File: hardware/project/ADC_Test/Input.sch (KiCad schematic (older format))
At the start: 51 parts, among them K601 HE3621A0510, K602 HE3621A0510, K603 HE3621A0510, Q601 BC847W, Q602 BC857W, U601 DG211, U602 DG211, U603 LTC1052, U604 TL061, U605 TL061, U606 TL431DBZ, U607 TL431DBZ, U608 LT5400-9k-1k

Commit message: Schematic design.
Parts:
- removed C? (x3): 10p, symbol Device:C
- removed Q? (x3): BC847W, Package_TO_SOT_SMD:SOT-323_SC-70, symbol Transistor_BJT:BC847W
- removed R? (x3): R, symbol Device:R
- added C601, C602, C603, C604, C605, C606, C607, C608, C609, C611, C612, C613, C614, C615, C616, C617, C619, C620, C622, C623, C624: 100n, Capacitor_SMD:C_0603_1608Metric_Pad1.05x0.95mm_HandSolder, symbol Device:C
- added R611, R613, R614, R615, R616, R617, R618: 620, Resistor_SMD:R_0603_1608Metric_Pad1.05x0.95mm_HandSolder, symbol Device:R
- added U603, U604, U605: SN74LVC1T45DBV, Package_TO_SOT_SMD:SOT-23-6, symbol Logic_LevelTranslator:SN74LVC1T45DBV
- added U606, U607: 74HCT595, Package_SO:TSSOP-16_4.4x5mm_P0.65mm, symbol 74xx:74HCT595
- C610: renamed from C601; footprint (none) -> Capacitor_SMD:C_1206_3216Metric_Pad1.42x1.75mm_HandSolder
- C618: renamed from C602; footprint (none) -> Capacitor_SMD:C_0603_1608Metric_Pad1.05x0.95mm_HandSolder
- C621: renamed from C603; footprint (none) -> Capacitor_SMD:C_0603_1608Metric_Pad1.05x0.95mm_HandSolder
- C625: renamed from C604; footprint (none) -> Capacitor_SMD:C_0603_1608Metric_Pad1.05x0.95mm_HandSolder
- C626: renamed from C605; footprint (none) -> Capacitor_SMD:C_0603_1608Metric_Pad1.05x0.95mm_HandSolder
- K601, K602, K603: footprint (none) -> ADC_Test:HE360_x-5050462-8
- L601: value INDUCTOR -> L0805R100MPWRT; footprint (none) -> Resistor_SMD:R_0805_2012Metric_Pad1.15x1.40mm_HandSolder
- R601, R602, R603, R604, R605, R606, R607: footprint (none) -> Resistor_SMD:R_1206_3216Metric_Pad1.42x1.75mm_HandSolder
- R608: renamed from R609; footprint (none) -> Resistor_SMD:R_1206_3216Metric_Pad1.42x1.75mm_HandSolder
- R609: renamed from R610; footprint (none) -> Resistor_SMD:R_1206_3216Metric_Pad1.42x1.75mm_HandSolder
- R610: renamed from R614; footprint (none) -> Resistor_SMD:R_1206_3216Metric_Pad1.42x1.75mm_HandSolder
- R612: value 1M -> 620; footprint (none) -> Resistor_SMD:R_0603_1608Metric_Pad1.05x0.95mm_HandSolder
- R619: renamed from R608; footprint (none) -> Resistor_SMD:R_0805_2012Metric_Pad1.15x1.40mm_HandSolder
- R620: renamed from R611; footprint (none) -> Resistor_SMD:R_0805_2012Metric_Pad1.15x1.40mm_HandSolder
- R621: renamed from R613; footprint (none) -> Resistor_SMD:R_0805_2012Metric_Pad1.15x1.40mm_HandSolder
- R622: renamed from R615; value 22 -> 22/.1%; footprint (none) -> Resistor_SMD:R_1206_3216Metric_Pad1.42x1.75mm_HandSolder
- R623: renamed from R616; value 12k -> 12k/.05%; footprint (none) -> Resistor_SMD:R_0603_1608Metric_Pad1.05x0.95mm_HandSolder
- R624: renamed from R617; footprint (none) -> Resistor_SMD:R_0805_2012Metric_Pad1.15x1.40mm_HandSolder
- R625: renamed from R618; footprint (none) -> Resistor_SMD:R_0805_2012Metric_Pad1.15x1.40mm_HandSolder
- R626: renamed from R619; footprint (none) -> Resistor_SMD:R_0805_2012Metric_Pad1.15x1.40mm_HandSolder
- R627: renamed from R620; footprint (none) -> Resistor_SMD:R_0805_2012Metric_Pad1.15x1.40mm_HandSolder
- R628: renamed from R621; footprint (none) -> Resistor_SMD:R_0805_2012Metric_Pad1.15x1.40mm_HandSolder
- R629: renamed from R622; footprint (none) -> Resistor_SMD:R_0805_2012Metric_Pad1.15x1.40mm_HandSolder
- R630: renamed from R623; value 620 -> 620/.05%; footprint (none) -> Resistor_SMD:R_0603_1608Metric_Pad1.05x0.95mm_HandSolder
- U601, U602: value DG211 -> DG211B; footprint (none) -> Package_SO:SOIC-16_3.9x9.9mm_P1.27mm; symbol ADC_TEST:DG211CJD -> ADC_TEST:DG211
- U601, U602: value DG211 -> DG211B; footprint (none) -> Package_SO:SOIC-16_3.9x9.9mm_P1.27mm
- U608: renamed from U603; footprint (none) -> Package_DIP:DIP-8_W7.62mm_Socket
- U609: renamed from U604; footprint (none) -> Package_SO:SOIC-8_3.9x4.9mm_P1.27mm
- U610: renamed from U605; footprint (none) -> Package_SO:SOIC-8_3.9x4.9mm_P1.27mm
- U613: renamed from U608; footprint (none) -> Package_SO:MSOP-8-1EP_3x3mm_P0.65mm_EP1.73x1.85mm_ThermalVias
- renumbered U606 to U611, U607 to U612
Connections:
- net labels added: +3.3VF, ADIN, DGNDF, K1_CTR, K2_CTR, K3_CTR, M1_2, M1_3, M1_4, M2_1, M2_2, M2_3, M2_4, SR_CLK, SR_DAT, SR_LAT
- net labels removed: AMP_OUT
- wire segments 165 -> 317
- no-connect marks 6 -> 12
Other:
- note added: "C1206C472FAGECTU"
- moved on the sheet: K601A, K601B, K602A, K602B, K603B, L601, R601, R602, R603, R604, R605, R606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

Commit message: Replaced TL061 with AD711.
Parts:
- removed U609, U610: TL061, Package_SO:SOIC-8_3.9x4.9mm_P1.27mm, symbol Amplifier_Operational:TL061
- added U609, U610: AD711, Package_SO:SOIC-8_3.9x4.9mm_P1.27mm, symbol ADC_TEST:AD711
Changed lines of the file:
@@
 Wire Wire Line
 	12450 4450 12900 4450
-$Comp
-L Amplifier_Operational:TL061 U610
-U 1 1 60D2E6C2
-P 12250 2350
-F 0 "U610" H 12350 2600 50  0000 L CNN
-F 1 "TL061" H 12350 2500 50  0000 L CNN
-F 2 "Package_SO:SOIC-8_3.9x4.9mm_P1.27mm" H 12300 2400 50  0001 C CNN
-F 3 "http://www.ti.com/lit/ds/symlink/tl061.pdf" H 12400 2500 50  0001 C CNN
-	1    12250 2350
-	1    0    0    -1
-$EndComp
 NoConn ~ 12250 2650
-NoConn ~ 12350 2650
 Wire Wire Line
 	11950 2450 11900 2450
@@
 	11450 6300 11900 6300
 $Comp
-L Amplifier_Operational:TL061 U609
-U 1 1 60E8A8A8
-P 10950 6300
-F 0 "U609" H 11000 6550 50  0000 L CNN
-F 1 "TL061" H 11000 6450 50  0000 L CNN
-F 2 "Package_SO:SOIC-8_3.9x4.9mm_P1.27mm" H 11000 6350 50  0001 C CNN
-F 3 "http://www.ti.com/lit/ds/symlink/tl061.pdf" H 11100 6450 50  0001 C CNN
-	1    10950 6300
-	1    0    0    -1
-$EndComp
-$Comp
 L Device:R R623
 U 1 1 60EAC183
@@
 Connection ~ 9450 6950
 NoConn ~ 10950 6600
-NoConn ~ 11050 6600
+NoConn ~ 10950 6000
 $Comp
 L ADC_TEST:+18VF #PWR0649
@@
 Text Notes 5900 6400 0    50   ~ 0
 C1206C472FAGECTU
+$Comp
+L ADC_TEST:AD711 U609
+U 1 1 5F856CB7
+P 10950 6300
+F 0 "U609" H 11100 6550 50  0000 L CNN
+F 1 "AD711" H 11100 6450 50  0000 L CNN
+F 2 "Package_SO:SOIC-8_3.9x4.9mm_P1.27mm" H 11000 6350 50  0001 C CNN
+F 3 "" H 11000 6450 50  0001 C CNN
+	1    10950 6300
+	1    0    0    -1
+$EndComp
+$Comp
+L ADC_TEST:AD711 U610
+U 1 1 5F86503E
+P 12250 2350
+F 0 "U610" H 12400 2600 50  0000 L CNN
+F 1 "AD711" H 12400 2500 50  0000 L CNN
+F 2 "Package_SO:SOIC-8_3.9x4.9mm_P1.27mm" H 12300 2400 50  0001 C CNN
+F 3 "" H 12300 2500 50  0001 C CNN
+	1    12250 2350
+	1    0    0    -1
+$EndComp
+NoConn ~ 12250 2050
 $EndSCHEMATC

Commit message: Schematic, PCB and BOM.
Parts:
- removed Q601: BC847W, Package_TO_SOT_SMD:SOT-323_SC-70, symbol Transistor_BJT:BC847W
- removed Q602: BC857W, Package_TO_SOT_SMD:SOT-323_SC-70, symbol Transistor_BJT:BC857W
- added Q601: BC847, Package_TO_SOT_SMD:SOT-23, symbol Transistor_BJT:BC847
- added Q602: BC857, Package_TO_SOT_SMD:SOT-23, symbol Transistor_BJT:BC857
- K601, K602, K603: footprint ADC_Test:HE360_x-5050462-8 -> ADC_TEST:HE360_x-5050462-8
- R601, R602, R603, R604, R605, R606, R607, R608, R609, R610: footprint Resistor_SMD:R_1206_3216Metric_Pad1.42x1.75mm_HandSolder -> Resistor_SMD:R_0805_2012Metric_Pad1.15x1.40mm_HandSolder
- R620, R621: value 240k -> 240k/.05%
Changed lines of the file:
@@
 P 7050 6100
 F 0 "R621" V 6843 6100 50  0000 C CNN
-F 1 "240k" V 6934 6100 50  0000 C CNN
+F 1 "240k/.05%" V 6934 6100 50  0000 C CNN
 F 2 "Resistor_SMD:R_0805_2012Metric_Pad1.15x1.40mm_HandSolder" V 6980 6100 50  0001 C CNN
 F 3 "~" H 7050 6100 50  0001 C CNN
@@
 P 6500 6100
 F 0 "R620" V 6293 6100 50  0000 C CNN
-F 1 "240k" V 6384 6100 50  0000 C CNN
+F 1 "240k/.05%" V 6384 6100 50  0000 C CNN
 F 2 "Resistor_SMD:R_0805_2012Metric_Pad1.15x1.40mm_HandSolder" V 6430 6100 50  0001 C CNN
 F 3 "~" H 6500 6100 50  0001 C CNN
@@
 F 0 "R601" V 2393 6750 50  0000 C CNN
 F 1 "1M" V 2484 6750 50  0000 C CNN
-F 2 "Resistor_SMD:R_1206_3216Metric_Pad1.42x1.75mm_HandSolder" V 2530 6750 50  0001 C CNN
+F 2 "Resistor_SMD:R_0805_2012Metric_Pad1.15x1.40mm_HandSolder" V 2530 6750 50  0001 C CNN
 F 3 "~" H 2600 6750 50  0001 C CNN
 	1    2600 6750
@@
 F 0 "R602" V 2693 6750 50  0000 C CNN
 F 1 "1M" V 2784 6750 50  0000 C CNN
-F 2 "Resistor_SMD:R_1206_3216Metric_Pad1.42x1.75mm_HandSolder" V 2830 6750 50  0001 C CNN
+F 2 "Resistor_SMD:R_0805_2012Metric_Pad1.15x1.40mm_HandSolder" V 2830 6750 50  0001 C CNN
 F 3 "~" H 2900 6750 50  0001 C CNN
 	1    2900 6750
@@
 F 0 "R603" V 2993 6750 50  0000 C CNN
 F 1 "1M" V 3084 6750 50  0000 C CNN
-F 2 "Resistor_SMD:R_1206_3216Metric_Pad1.42x1.75mm_HandSolder" V 3130 6750 50  0001 C CNN
+F 2 "Resistor_SMD:R_0805_2012Metric_Pad1.15x1.40mm_HandSolder" V 3130 6750 50  0001 C CNN
 F 3 "~" H 3200 6750 50  0001 C CNN
 	1    3200 6750
@@
 F 0 "R604" V 3293 6750 50  0000 C CNN
 F 1 "1M" V 3384 6750 50  0000 C CNN
-F 2 "Resistor_SMD:R_1206_3216Metric_Pad1.42x1.75mm_HandSolder" V 3430 6750 50  0001 C CNN
+F 2 "Resistor_SMD:R_0805_2012Metric_Pad1.15x1.40mm_HandSolder" V 3430 6750 50  0001 C CNN
 F 3 "~" H 3500 6750 50  0001 C CNN
 	1    3500 6750
@@
 F 0 "R605" V 3593 6750 50  0000 C CNN
 F 1 "1M" V 3684 6750 50  0000 C CNN
-F 2 "Resistor_SMD:R_1206_3216Metric_Pad1.42x1.75mm_HandSolder" V 3730 6750 50  0001 C CNN
+F 2 "Resistor_SMD:R_0805_2012Metric_Pad1.15x1.40mm_HandSolder" V 3730 6750 50  0001 C CNN
 F 3 "~" H 3800 6750 50  0001 C CNN
 	1    3800 6750
@@
 F 0 "R606" V 3893 6750 50  0000 C CNN
 F 1 "1M" V 3984 6750 50  0000 C CNN
-F 2 "Resistor_SMD:R_1206_3216Metric_Pad1.42x1.75mm_HandSolder" V 4030 6750 50  0001 C CNN
+F 2 "Resistor_SMD:R_0805_2012Metric_Pad1.15x1.40mm_HandSolder" V 4030 6750 50  0001 C CNN
 F 3 "~" H 4100 6750 50  0001 C CNN
 	1    4100 6750
@@
 F 0 "R607" V 4193 6750 50  0000 C CNN
 F 1 "1M" V 4284 6750 50  0000 C CNN
-F 2 "Resistor_SMD:R_1206_3216Metric_Pad1.42x1.75mm_HandSolder" V 4330 6750 50  0001 C CNN
+F 2 "Resistor_SMD:R_0805_2012Metric_Pad1.15x1.40mm_HandSolder" V 4330 6750 50  0001 C CNN
 F 3 "~" H 4400 6750 50  0001 C CNN
 	1    4400 6750
@@
 F 0 "R608" V 4493 6750 50  0000 C CNN
 F 1 "1M" V 4584 6750 50  0000 C CNN
-F 2 "Resistor_SMD:R_1206_3216Metric_Pad1.42x1.75mm_HandSolder" V 4630 6750 50  0001 C CNN
+F 2 "Resistor_SMD:R_0805_2012Metric_Pad1.15x1.40mm_HandSolder" V 4630 6750 50  0001 C CNN
 F 3 "~" H 4700 6750 50  0001 C CNN
 	1    4700 6750
@@
 F 0 "R609" V 4793 6750 50  0000 C CNN
 F 1 "1M" V 4884 6750 50  0000 C CNN
-F 2 "Resistor_SMD:R_1206_3216Metric_Pad1.42x1.75mm_HandSolder" V 4930 6750 50  0001 C CNN
+F 2 "Resistor_SMD:R_0805_2012Metric_Pad1.15x1.40mm_HandSolder" V 4930 6750 50  0001 C CNN
 F 3 "~" H 5000 6750 50  0001 C CNN
 	1    5000 6750
@@
 F 0 "R610" H 5320 7046 50  0000 L CNN
 F 1 "1M" H 5320 6955 50  0000 L CNN
-F 2 "Resistor_SMD:R_1206_3216Metric_Pad1.42x1.75mm_HandSolder" V 5180 7000 50  0001 C CNN
+F 2 "Resistor_SMD:R_0805_2012Metric_Pad1.15x1.40mm_HandSolder" V 5180 7000 50  0001 C CNN
 F 3 "~" H 5250 7000 50  0001 C CNN
 	1    5250 7000
@@
 Wire Wire Line
 	12650 2350 12550 2350
-$Comp
-L Transistor_BJT:BC857W Q602
-U 1 1 60D373EE
-P 12250 3200
-F 0 "Q602" H 12441 3154 50  0000 L CNN
-F 1 "BC857W" H 12441 3245 50  0000 L CNN
-F 2 "Package_TO_SOT_SMD:SOT-323_SC-70" H 12450 3125 50  0001 L CIN
-F 3 "http://www.infineon.com/dgdl/Infineon-BC857SERIES_BC858SERIES_BC859SERIES_BC860SERIES-DS-v01_01-en.pdf?fileId=db3a304314dca389011541da0e3a1661" H 12250 3200 50  0001 L CNN
-	1    12250 3200
-	-1   0    0    1
-$EndComp
 $Comp
 L ADC_TEST:-18VF #PWR0655
@@
 	13050 1350 13050 1600
 Connection ~ 13050 1600
-$Comp
-L Transistor_BJT:BC847W Q601
-U 1 1 60D5EC24
-P 12250 1600
-F 0 "Q601" H 12441 1646 50  0000 L CNN
-F 1 "BC847W" H 12441 1555 50  0000 L CNN
-F 2 "Package_TO_SOT_SMD:SOT-323_SC-70" H 12450 1525 50  0001 L CIN
-F 3 "http://www.infineon.com/dgdl/Infineon-BC847SERIES_BC848SERIES_BC849SERIES_BC850SERIES-DS-v01_01-en.pdf?fileId=db3a304314dca389011541d4630a1657" H 12250 1600 50  0001 L CNN
-	1    12250 1600
-	-1   0    0    -1
-$EndComp
 Wire Wire Line
 	12150 1800 12150 1900
@@
 F 0 "K601" V 2315 6100 50  0000 C CNN
 F 1 "HE3621A0510" V 2224 6100 50  0000 C CNN
-F 2 "ADC_Test:HE360_x-5050462-8" H 2350 6050 50  0001 C CNN
+F 2 "ADC_TEST:HE360_x-5050462-8" H 2350 6050 50  0001 C CNN
 F 3 "" H 2350 6050 50  0001 C CNN
 	1    2100 6100
@@
 F 0 "K601" H 2478 10396 50  0000 L CNN
 F 1 "HE3621A0510" H 2478 10305 50  0000 L CNN
-F 2 "ADC_Test:HE360_x-5050462-8" H 2650 10300 50  0001 C CNN
+F 2 "ADC_TEST:HE360_x-5050462-8" H 2650 10300 50  0001 C CNN
 F 3 "" H 2650 10300 50  0001 C CNN
 	2    2400 10350
@@
 F 0 "K602" V 2315 6750 50  0000 C CNN
 F 1 "HE3621A0510" V 2224 6750 50  0000 C CNN
-F 2 "ADC_Test:HE360_x-5050462-8" H 2350 6700 50  0001 C CNN
+F 2 "ADC_TEST:HE360_x-5050462-8" H 2350 6700 50  0001 C CNN
 F 3 "" H 2350 6700 50  0001 C CNN
 	1    2100 6750
@@
 F 0 "K602" H 3278 10396 50  0000 L CNN
 F 1 "HE3621A0510" H 3278 10305 50  0000 L CNN
-F 2 "ADC_Test:HE360_x-5050462-8" H 3450 10300 50  0001 C CNN
+F 2 "ADC_TEST:HE360_x-5050462-8" H 3450 10300 50  0001 C CNN
 F 3 "" H 3450 10300 50  0001 C CNN
 	2    3200 10350
@@
 F 0 "K603" H 5328 6446 50  0000 L CNN
 F 1 "HE3621A0510" H 5328 6355 50  0000 L CNN
-F 2 "ADC_Test:HE360_x-5050462-8" H 5500 6350 50  0001 C CNN
+F 2 "ADC_TEST:HE360_x-5050462-8" H 5500 6350 50  0001 C CNN
 F 3 "" H 5500 6350 50  0001 C CNN
 	1    5250 6400
@@
 F 0 "K603" H 4078 10396 50  0000 L CNN
 F 1 "HE3621A0510" H 4078 10305 50  0000 L CNN
-F 2 "ADC_Test:HE360_x-5050462-8" H 4250 10300 50  0001 C CNN
+F 2 "ADC_TEST:HE360_x-5050462-8" H 4250 10300 50  0001 C CNN
 F 3 "" H 4250 10300 50  0001 C CNN
 	2    4000 10350
@@
 $EndComp
 NoConn ~ 12250 2050
+$Comp
+L Transistor_BJT:BC847 Q601
+U 1 1 5F8E554E
+P 12250 1600
+F 0 "Q601" H 12441 1646 50  0000 L CNN
+F 1 "BC847" H 12441 1555 50  0000 L CNN
+F 2 "Package_TO_SOT_SMD:SOT-23" H 12450 1525 50  0001 L CIN
+F 3 "http://www.infineon.com/dgdl/Infineon-BC847SERIES_BC848SERIES_BC849SERIES_BC850SERIES-DS-v01_01-en.pdf?fileId=db3a304314dca389011541d4630a1657" H 12250 1600 50  0001 L CNN
+	1    12250 1600
+	-1   0    0    -1
+$EndComp
+$Comp
+L Transistor_BJT:BC857 Q602
+U 1 1 5F8EBE07
+P 12250 3200
+F 0 "Q602" H 12441 3154 50  0000 L CNN
+F 1 "BC857" H 12441 3245 50  0000 L CNN
+F 2 "Package_TO_SOT_SMD:SOT-23" H 12450 3125 50  0001 L CIN
+F 3 "http://www.fairchildsemi.com/ds/BC/BC856.pdf" H 12250 3200 50  0001 L CNN
+	1    12250 3200
+	-1   0    0    1
+$EndComp
 $EndSCHEMATC

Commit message: PCB design
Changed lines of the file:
@@
-$Comp
-L ADC_TEST:HE3621A0510 K603
-U 1 1 6104A372
-P 5250 6400
-F 0 "K603" H 5328 6446 50  0000 L CNN
-F 1 "HE3621A0510" H 5328 6355 50  0000 L CNN
-F 2 "ADC_TEST:HE360_x-5050462-8" H 5500 6350 50  0001 C CNN
-F 3 "" H 5500 6350 50  0001 C CNN
-	1    5250 6400
-	1    0    0    -1
-$EndComp
 $Comp
 L ADC_TEST:HE3621A0510 K603
@@
 	-1   0    0    1
 $EndComp
+$Comp
+L ADC_TEST:HE3621A0510 K603
+U 1 1 6104A372
+P 5250 6400
+F 0 "K603" H 5500 6450 50  0000 L CNN
+F 1 "HE3621A0510" H 5350 6350 50  0000 L CNN
+F 2 "ADC_TEST:HE360_x-5050462-8" H 5500 6350 50  0001 C CNN
+F 3 "" H 5500 6350 50  0001 C CNN
+	1    5250 6400
+	1    0    0    -1
+$EndComp
 $EndSCHEMATC

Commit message: PCB design.
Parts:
- removed C615: 100n, Capacitor_SMD:C_0603_1608Metric_Pad1.05x0.95mm_HandSolder, symbol Device:C
- renumbered C603 to C602, C602 to C603, C606 to C604, C604 to C605, C608 to C606, C605 to C607, C611 to C608, C607 to C609, C613 to C611, C609 to C612, C612 to C613, C616 to C615, C617 to C616, C618 to C617, C619 to C618, C620 to C619, C621 to C620, C622 to C621, C623 to C622, C624 to C623, C625 to C624, C626 to C625
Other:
- moved on the sheet: C601, C602, C603, C604, C605, C606, C607, C608, C609, C611, C612, C613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

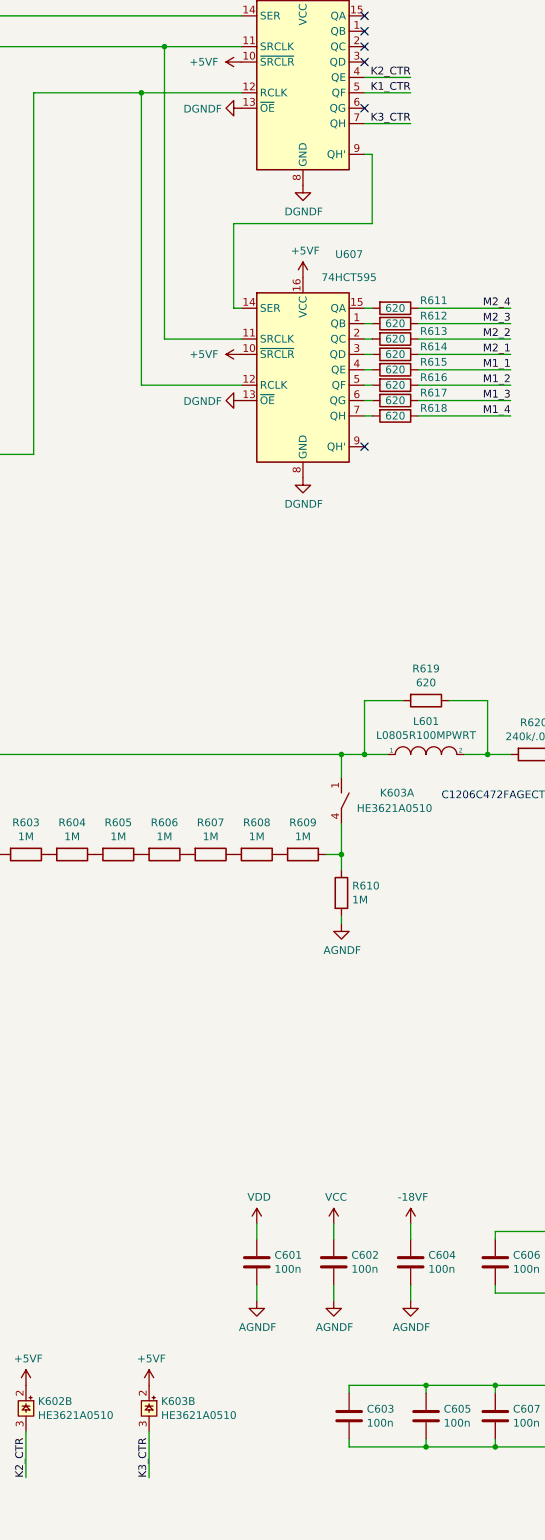
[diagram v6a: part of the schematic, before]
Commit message: MCU readout from FPGA works.
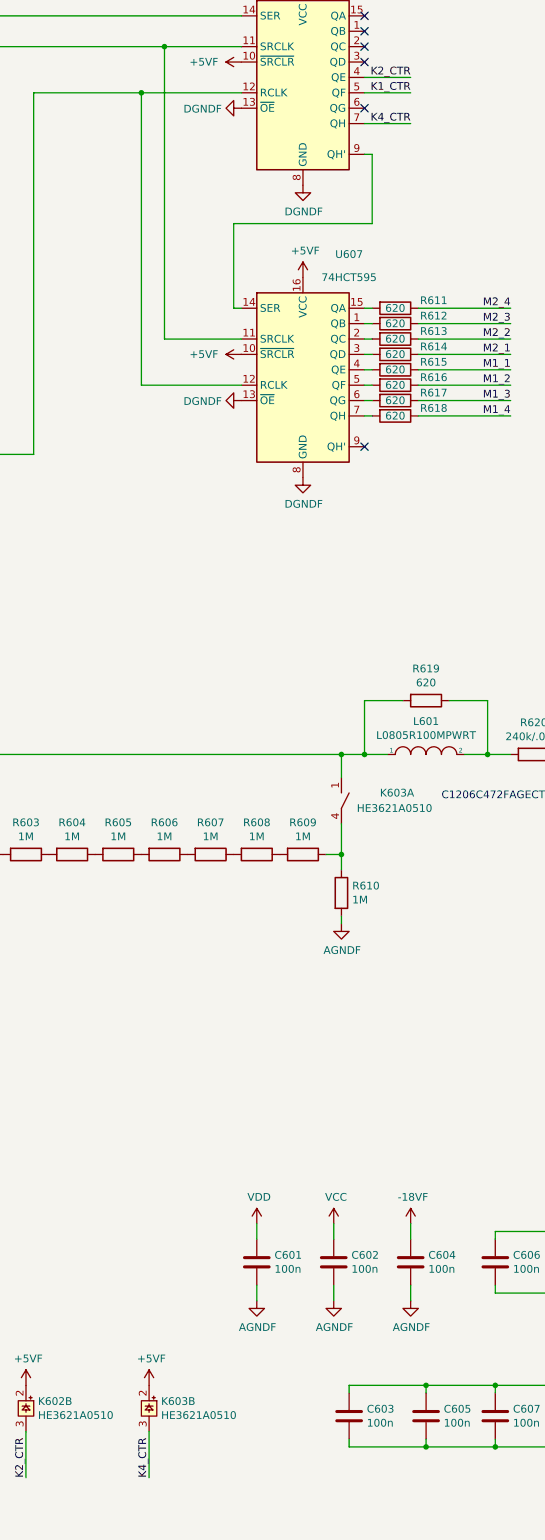
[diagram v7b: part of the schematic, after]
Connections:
- net K3_CTR renamed K4_CTR
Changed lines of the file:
@@
 	3200 10500 3200 10800
 Text Label 4000 10800 1    50   ~ 0
-K3_CTR
+K4_CTR
 Wire Wire Line
 	4000 10500 4000 10800
@@
 	5400 1700 5700 1700
 Text Label 5700 2000 2    50   ~ 0
-K3_CTR
+K4_CTR
 Wire Wire Line
 	5400 2000 5700 2000
